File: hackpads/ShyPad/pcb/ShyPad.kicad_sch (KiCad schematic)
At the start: 26 parts, among them SW1 SW_Push_45deg, SW10 SW_Push_45deg, SW11 SW_Push_45deg, SW12 SW_Push_45deg, SW2 SW_Push_45deg, SW3 RotaryEncoder_Switch_MP, SW4 SW_Push_45deg, SW5 SW_Push_45deg, SW6 SW_Push_45deg, SW7 SW_Push_45deg, SW8 SW_Push_45deg, SW9 SW_Push_45deg, U1 XIAO-RP2040-DIP

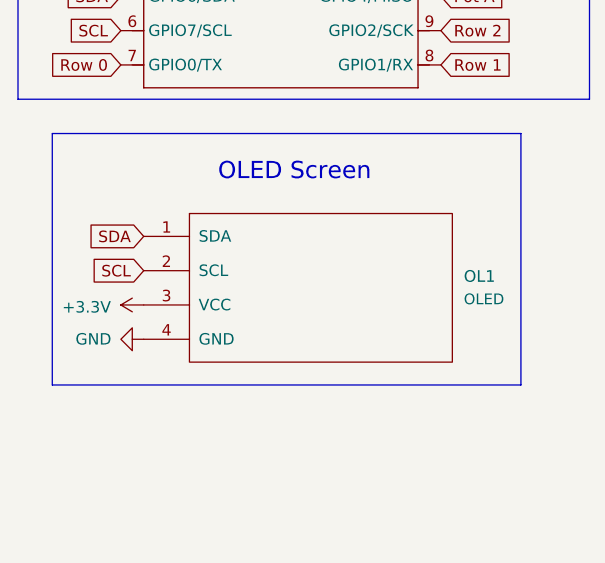
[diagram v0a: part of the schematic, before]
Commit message: fix flipped OLED pins + THICK power traces
the schematic was flipped for some reason
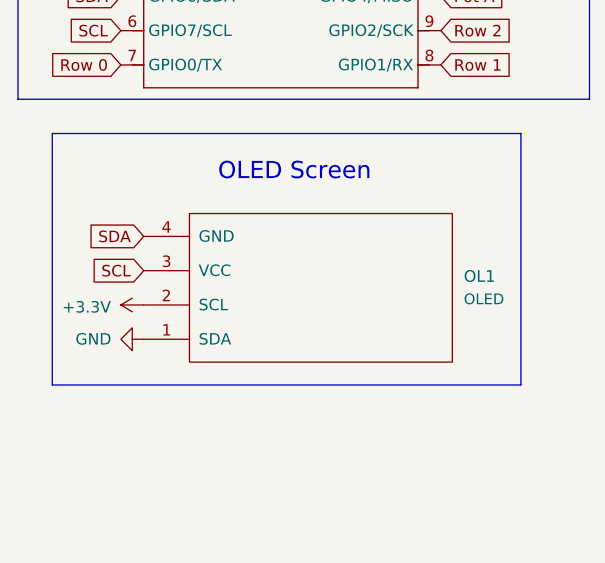
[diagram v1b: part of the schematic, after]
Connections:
- net +3.3V: now also OL1.2 (SCL); no longer OL1.3 (VCC)
- net GND: now also OL1.1 (SDA); no longer OL1.4 (GND)
- net SCL: now also OL1.3 (VCC); no longer OL1.2 (SCL)
- net SDA: now also OL1.4 (GND); no longer OL1.1 (SDA)
